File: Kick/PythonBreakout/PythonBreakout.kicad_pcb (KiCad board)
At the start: 4 copper layers, 128.8 x 67 mm, 16 parts, among them U0 NOIP1SN1300A-QTI

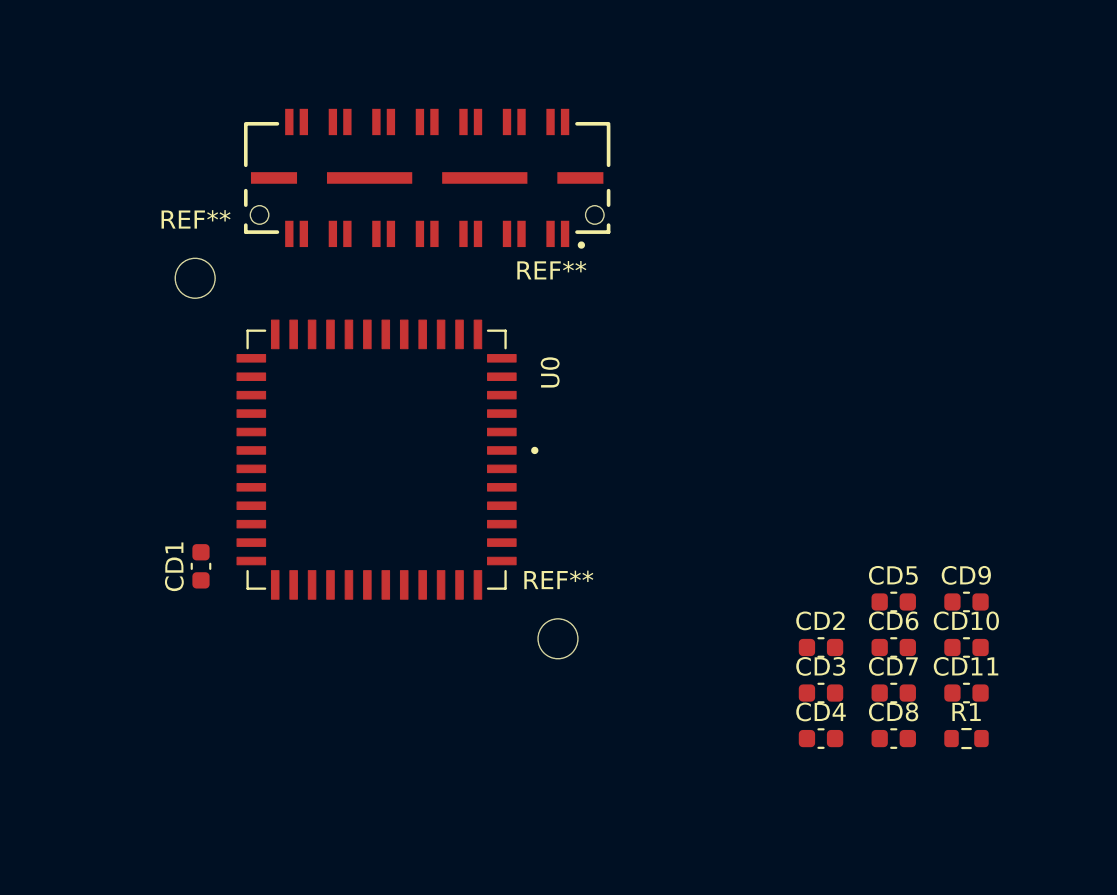
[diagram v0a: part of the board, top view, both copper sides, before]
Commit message: tried several connectors, chose TFML/SFML. routing LVDS witb 0 skew.
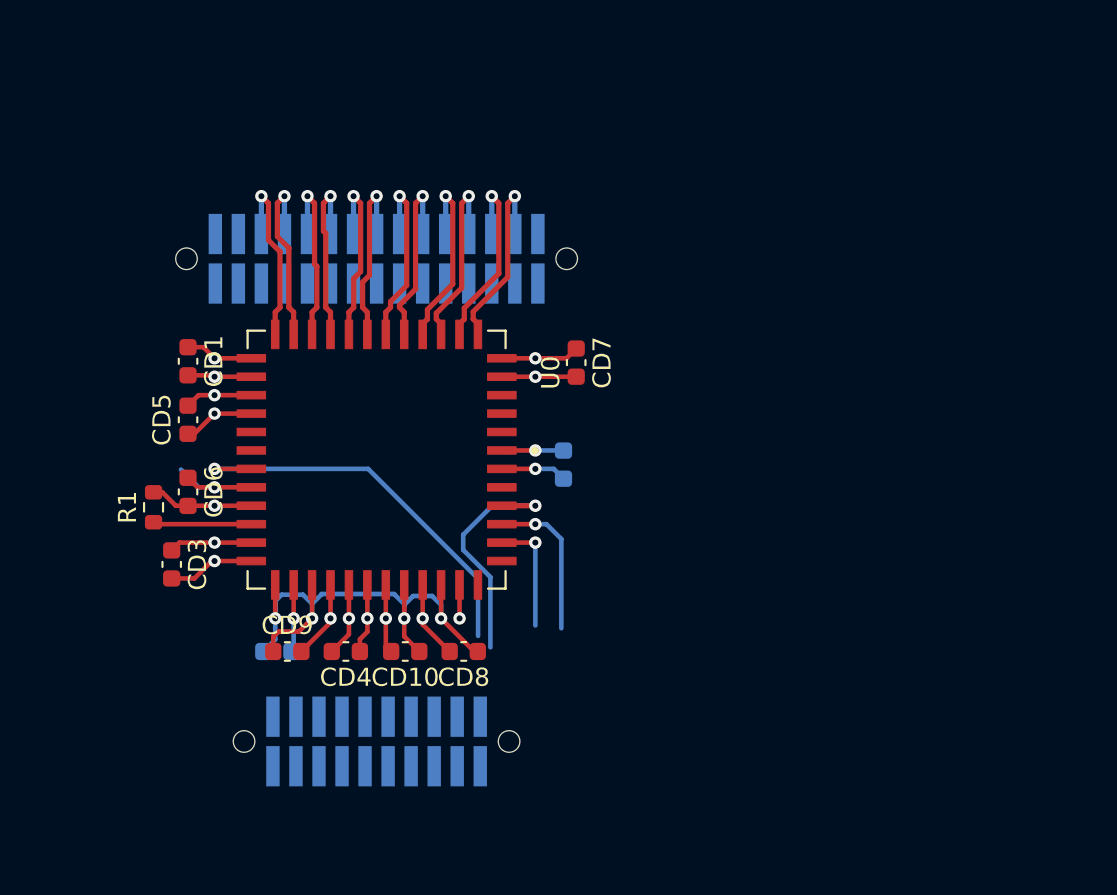
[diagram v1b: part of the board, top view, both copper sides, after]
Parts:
- removed REF**: SAMTEC_QTE-014-01-F-D-DP-A, SAMTEC_QTE01401FDDPA:SAMTEC_QTE-014-01-F-D-DP-A
- removed REF** (x2): MountingHole_2.2mm_M2, MountingHole:MountingHole_2.2mm_M2
- added J1: Conn_02x15_Odd_Even, SAMTEC_SFML11502LDLC:SAMTEC_SFML-115-02-L-D-LC, B.Cu at (90.0, 58.9)
- added J2: Conn_02x10_Odd_Even, SAMTEC_SFML11002LDLC:SAMTEC_SFML-110-02-L-D-LC, B.Cu at (90.0, 85.5)
- CD11, CD2: moved to B.Cu
- moved R1 46.6 mm to (77.7, 72.6), turned to 90 degrees
- moved CD5 40.2 mm to (79.6, 67.8), turned to 90 degrees
- moved CD6 39.8 mm to (79.6, 71.8), turned to -90 degrees
- moved CD11 38.1 mm to (84.5, 80.6)
- moved CD9 37.5 mm to (85.1, 80.6)
- moved CD3 36.5 mm to (78.7, 75.8), turned to -90 degrees
- moved CD10 30.9 mm to (91.6, 80.6), turned to 180 degrees
- moved CD4 26.6 mm to (88.3, 80.6), turned to 180 degrees
- moved CD7 25.3 mm to (101.0, 64.7), turned to -90 degrees
- moved CD8 24.2 mm to (94.8, 80.6), turned to 180 degrees
- moved CD2 17.4 mm to (100.3, 70.3), turned to -90 degrees
- moved CD1 11.3 mm to (79.6, 64.6), turned to -90 degrees
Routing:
- net /vdd33: track 0.00 -> 52.8 mm, vias 0 -> 4
- net GND: track 0.00 -> 45.7 mm, vias 0 -> 11
- net /vdd18: track 0.00 -> 38.4 mm, vias 0 -> 3
- net /vddpix: track 0.00 -> 31.4 mm, vias 0 -> 4
- net /noip_clk: track 0.00 -> 22.2 mm, vias 0 -> 1
- net /resetn: track 0.00 -> 13.3 mm, vias 0 -> 1
- net /clkout0_N: track 0.00 -> 10.8 mm, vias 0 -> 1
- net /clkout0_P: track 0.00 -> 10.8 mm, vias 0 -> 1
- net /dout0_P: track 0.00 -> 10.6 mm, vias 0 -> 1
- net /dout0_N: track 0.00 -> 10.6 mm, vias 0 -> 1
- net /dout1_N: track 0.00 -> 10.3 mm, vias 0 -> 1
- net /dout1_P: track 0.00 -> 10.3 mm, vias 0 -> 1
- net /sync0_N: track 0.00 -> 10.2 mm, vias 0 -> 1
- net /sync0_P: track 0.00 -> 10.2 mm, vias 0 -> 1
- net /dout2_P: track 0.00 -> 10.1 mm, vias 0 -> 1
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- added copper zone on In2.Cu, net GND
- removed copper zone on In2.Cu, net +3V3
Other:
- board text removed: "C"

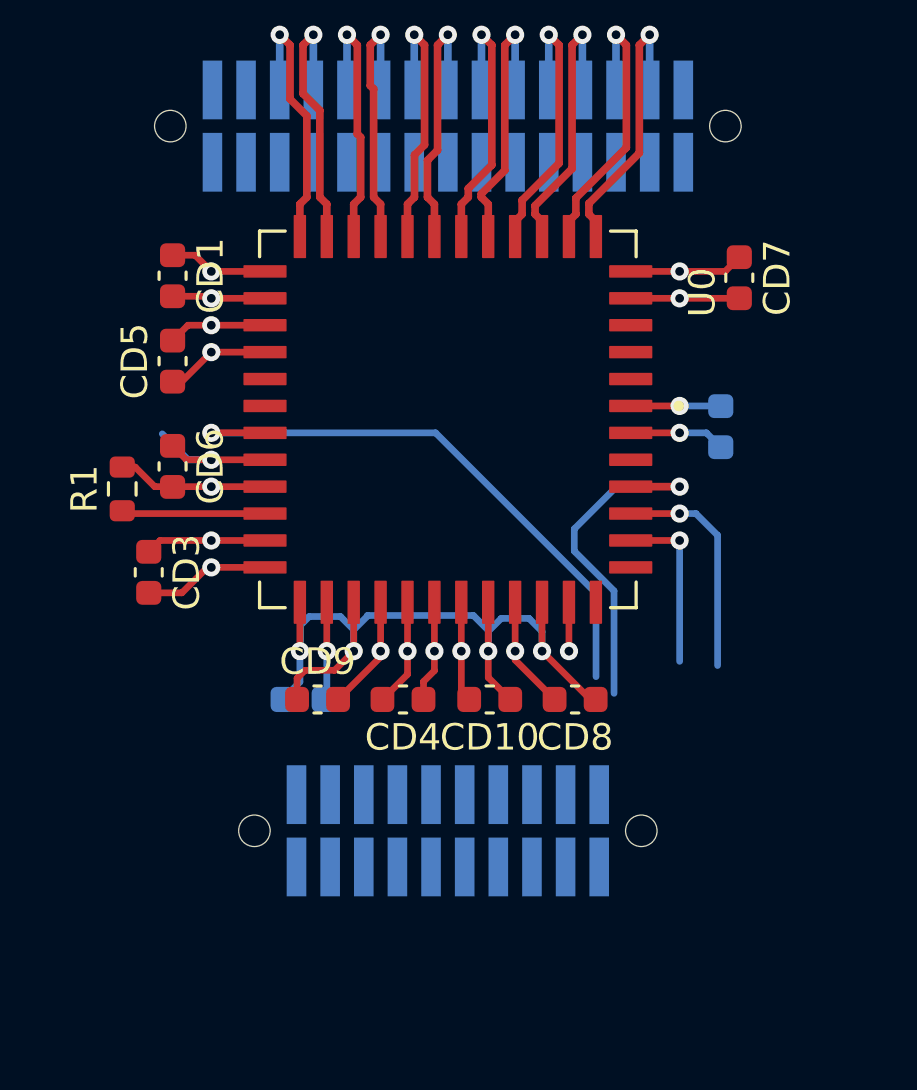
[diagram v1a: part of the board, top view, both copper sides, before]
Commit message: routed PythonBreakout with SFML
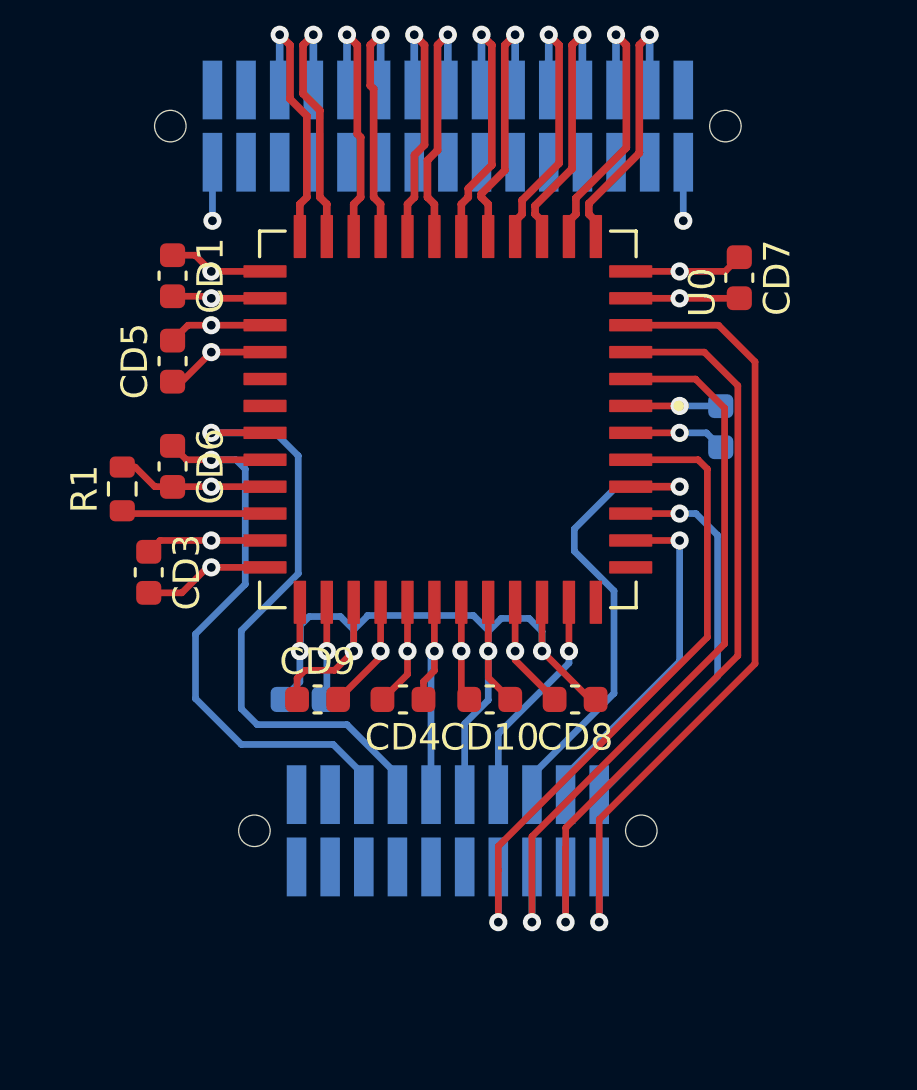
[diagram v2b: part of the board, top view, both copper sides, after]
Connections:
- J1 pad 2: unconnected-(J1-Pin_2-Pad2) -> GND
- J1 pad 30: unconnected-(J1-Pin_30-Pad30) -> GND
- J2 pad 1: unconnected-(J2-Pin_1-Pad1) -> /monitor1
- J2 pad 11: unconnected-(J2-Pin_11-Pad11) -> /vdd33
- J2 pad 13: unconnected-(J2-Pin_13-Pad13) -> /noip_clk
- J2 pad 15: unconnected-(J2-Pin_15-Pad15) -> /vdd18
- J2 pad 2: unconnected-(J2-Pin_2-Pad2) -> /sck
- J2 pad 3: unconnected-(J2-Pin_3-Pad3) -> /monitor0
- J2 pad 4: unconnected-(J2-Pin_4-Pad4) -> /miso
- J2 pad 5: unconnected-(J2-Pin_5-Pad5) -> /resetn
- J2 pad 6: unconnected-(J2-Pin_6-Pad6) -> /mosi
- J2 pad 7: unconnected-(J2-Pin_7-Pad7) -> /trigger0
- J2 pad 8: unconnected-(J2-Pin_8-Pad8) -> /ss_n
- J2 pad 9: unconnected-(J2-Pin_9-Pad9) -> /vddpix
- U0 pad 47: /ss -> /ss_n
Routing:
- net /sck: track 0.00 -> 30.9 mm, vias 0 -> 1
- net /miso: track 0.00 -> 29.6 mm, vias 0 -> 1
- net /mosi: track 0.00 -> 28.5 mm, vias 0 -> 1
- net /ss_n: track 0.00 -> 25.5 mm, vias 0 -> 1
- net /vdd18: track 38.4 -> 55.3 mm
- net /monitor0: track 6.41 -> 13.2 mm
- net /monitor1: track 8.54 -> 15.3 mm
- net /trigger0: track 1.85 -> 8.37 mm
- net /vddpix: track 31.4 -> 37.2 mm
- net /vdd33: track 52.8 -> 58.2 mm
- net /resetn: track 13.3 -> 18.4 mm
- net GND: track 45.7 -> 50.1 mm, vias 11 -> 13
- net /noip_clk: track 22.2 -> 23.8 mm

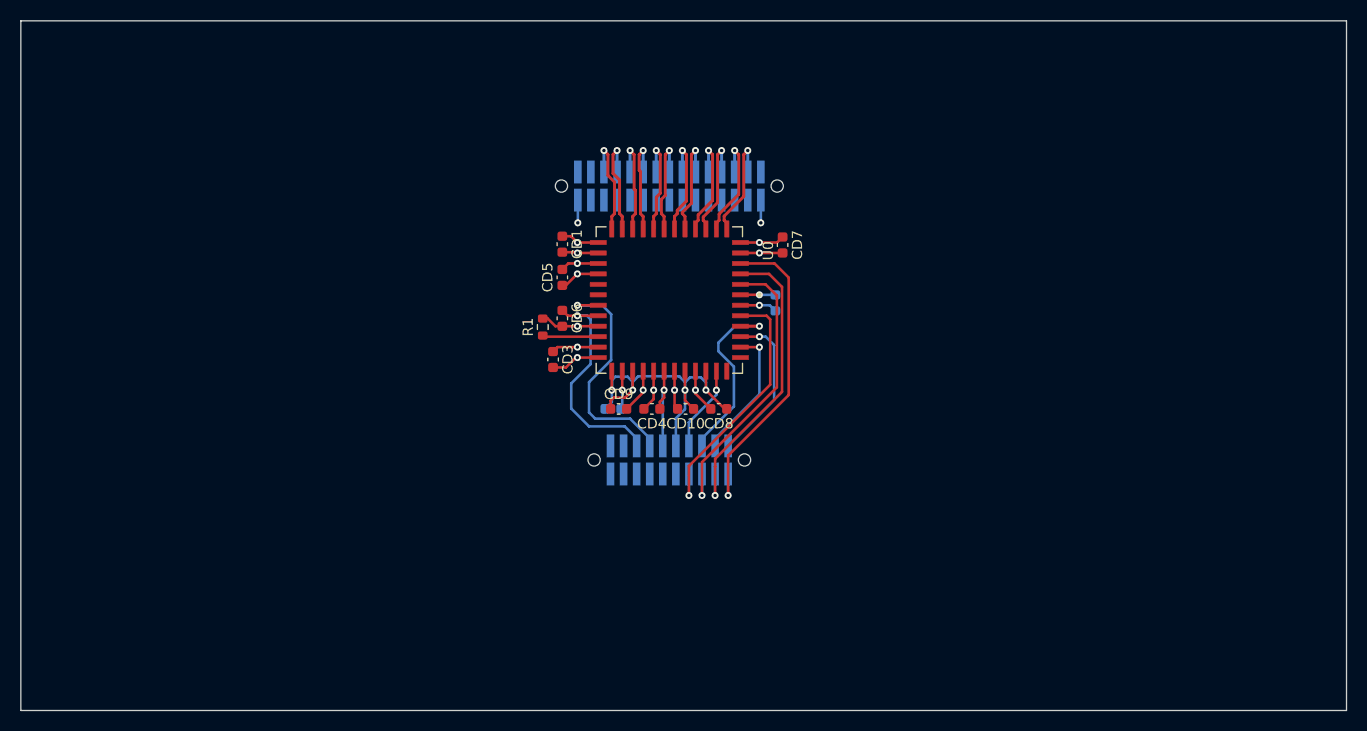
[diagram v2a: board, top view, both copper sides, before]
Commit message: routed 0 side on MainBoard with TFMLs
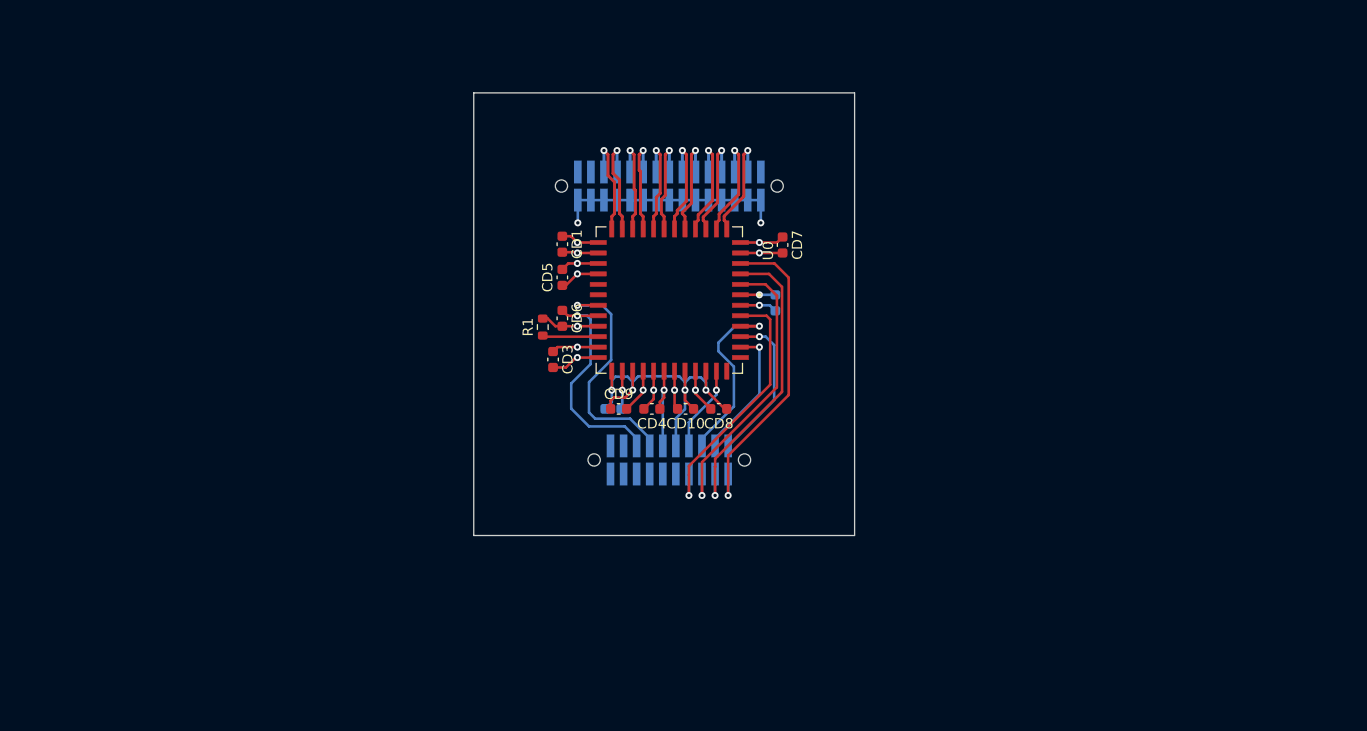
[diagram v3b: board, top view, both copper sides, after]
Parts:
- J1: value Conn_02x15_Odd_Even -> SFML-115-02
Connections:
- J1 pad 10: unconnected-(J1-Pin_10-Pad10) -> GND
- J1 pad 12: unconnected-(J1-Pin_12-Pad12) -> GND
- J1 pad 14: unconnected-(J1-Pin_14-Pad14) -> GND
- J1 pad 16: unconnected-(J1-Pin_16-Pad16) -> GND
- J1 pad 18: unconnected-(J1-Pin_18-Pad18) -> GND
- J1 pad 20: unconnected-(J1-Pin_20-Pad20) -> GND
- J1 pad 22: unconnected-(J1-Pin_22-Pad22) -> GND
- J1 pad 24: unconnected-(J1-Pin_24-Pad24) -> GND
- J1 pad 26: unconnected-(J1-Pin_26-Pad26) -> GND
- J1 pad 28: unconnected-(J1-Pin_28-Pad28) -> GND
- J1 pad 4: unconnected-(J1-Pin_4-Pad4) -> GND
- J1 pad 6: unconnected-(J1-Pin_6-Pad6) -> GND
- J1 pad 8: unconnected-(J1-Pin_8-Pad8) -> GND
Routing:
- net GND: track 50.1 -> 68.3 mm
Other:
- board size 128.8 x 67 mm -> 37 x 43 mm

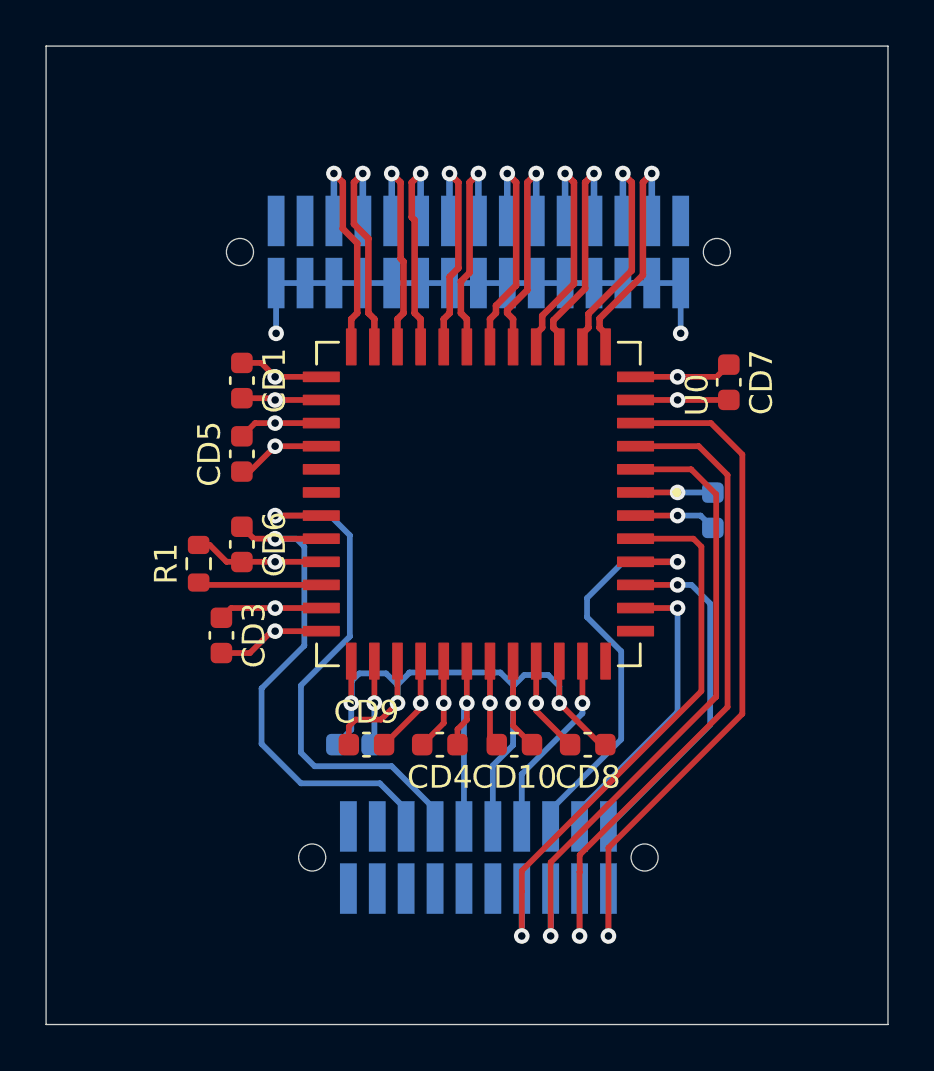
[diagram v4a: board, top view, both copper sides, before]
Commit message: routed all layers, length matched top part and updated models
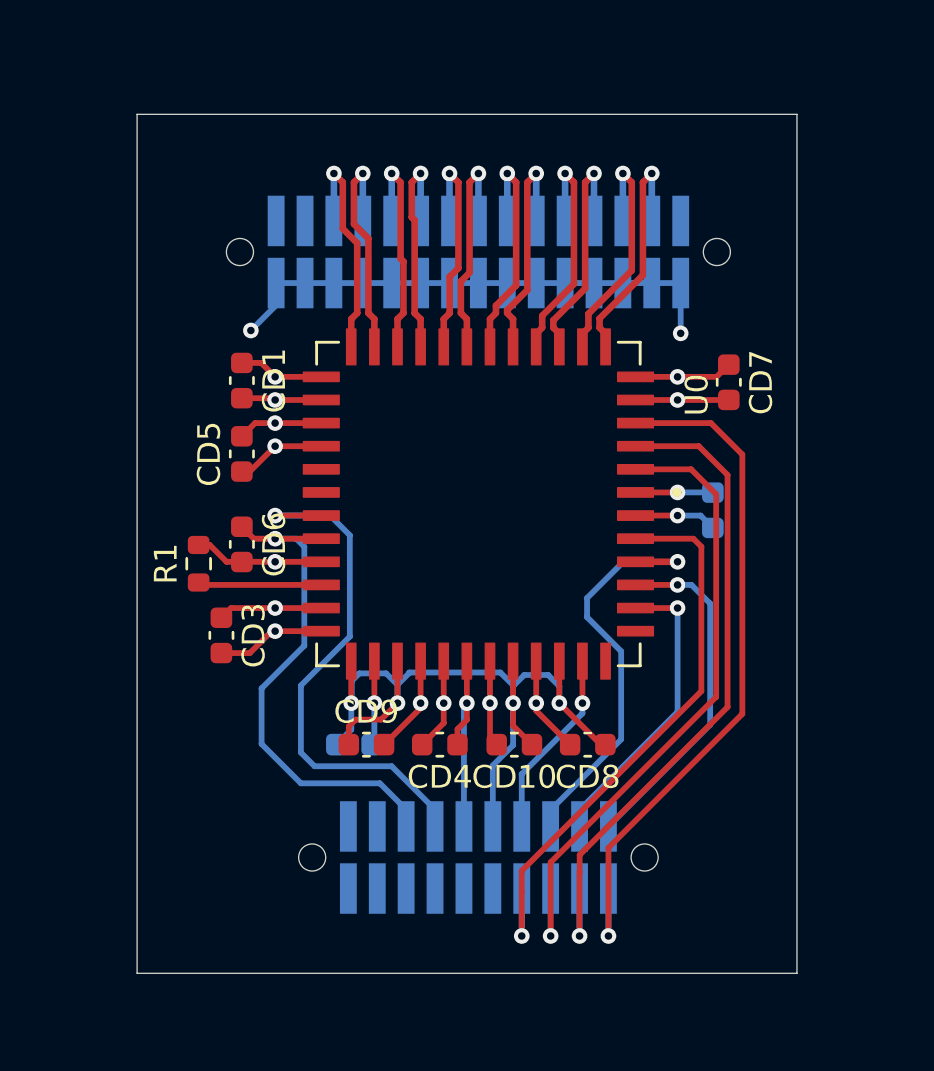
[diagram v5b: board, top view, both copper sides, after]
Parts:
- turned J1 to 0 degrees
- turned J2 to 0 degrees
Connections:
- J1 pad 1: unconnected-(J1-Pin_1-Pad1) -> GND
- J1 pad 10: GND -> /dout3_P
- J1 pad 11: /dout1_N -> GND
- J1 pad 12: GND -> /dout3_N
- J1 pad 13: /dout1_P -> GND
- J1 pad 14: GND -> /dout2_P
- J1 pad 15: /dout2_N -> GND
- J1 pad 16: GND -> /dout2_N
- J1 pad 17: /dout2_P -> GND
- J1 pad 18: GND -> /dout1_P
- J1 pad 19: /dout3_N -> GND
- J1 pad 2: GND -> unconnected-(J1-Pin_2-Pad2)
- J1 pad 20: GND -> /dout1_N
- J1 pad 21: /dout3_P -> GND
- J1 pad 22: GND -> /dout0_P
- J1 pad 23: /sync0_N -> GND
- J1 pad 24: GND -> /dout0_N
- J1 pad 25: /sync0_P -> GND
- J1 pad 26: GND -> /clkout0_P
- J1 pad 27: unconnected-(J1-Pin_27-Pad27) -> GND
- J1 pad 28: GND -> /clkout0_N
- J1 pad 29: unconnected-(J1-Pin_29-Pad29) -> GND
- J1 pad 3: /clkout0_N -> GND
- J1 pad 30: GND -> unconnected-(J1-Pin_30-Pad30)
- J1 pad 4: GND -> unconnected-(J1-Pin_4-Pad4)
- J1 pad 5: /clkout0_P -> GND
- J1 pad 6: GND -> /sync0_P
- J1 pad 7: /dout0_N -> GND
- J1 pad 8: GND -> /sync0_N
- J1 pad 9: /dout0_P -> GND
- J2 pad 1: /monitor1 -> unconnected-(J2-Pin_1-Pad1)
- J2 pad 10: unconnected-(J2-Pin_10-Pad10) -> /vdd33
- J2 pad 11: /vdd33 -> unconnected-(J2-Pin_11-Pad11)
- J2 pad 12: unconnected-(J2-Pin_12-Pad12) -> /vddpix
- J2 pad 13: /noip_clk -> /ss_n
- J2 pad 14: unconnected-(J2-Pin_14-Pad14) -> /trigger0
- J2 pad 15: /vdd18 -> /mosi
- J2 pad 16: unconnected-(J2-Pin_16-Pad16) -> /resetn
- J2 pad 17: unconnected-(J2-Pin_17-Pad17) -> /miso
- J2 pad 18: unconnected-(J2-Pin_18-Pad18) -> /monitor0
- J2 pad 19: unconnected-(J2-Pin_19-Pad19) -> /sck
- J2 pad 2: /sck -> unconnected-(J2-Pin_2-Pad2)
- J2 pad 20: unconnected-(J2-Pin_20-Pad20) -> /monitor1
- J2 pad 3: /monitor0 -> unconnected-(J2-Pin_3-Pad3)
- J2 pad 4: /miso -> unconnected-(J2-Pin_4-Pad4)
- J2 pad 5: /resetn -> unconnected-(J2-Pin_5-Pad5)
- J2 pad 6: /mosi -> /vdd18
- J2 pad 7: /trigger0 -> unconnected-(J2-Pin_7-Pad7)
- J2 pad 8: /ss_n -> /noip_clk
- J2 pad 9: /vddpix -> unconnected-(J2-Pin_9-Pad9)
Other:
- board size 37 x 43 mm -> 29 x 37.8 mm
